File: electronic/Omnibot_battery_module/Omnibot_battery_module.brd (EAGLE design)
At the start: 60 x 213.7 mm, 30 parts, among them IC7 TJA1050T, J1 B1, J3 XT60-M, J4 XT60-M, J7 ATX24RH, J9 RES JUMPER, Y1 CSTCE16M0V53-R0

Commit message: add manip, realseses, fix battery module
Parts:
- moved J11 3.81 mm to (41.9, -8.89)
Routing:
- net GND: track 410.4 -> 415.5 mm
- net N$26: track 42.5 -> 38.7 mm
- net N$25: track 42.6 -> 38.8 mm
- net N$24: track 40.1 -> 36.3 mm
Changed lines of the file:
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@@
 <attribute name="VALUE" x="51.054" y="95.25" size="0.6096" layer="27" font="vector" ratio="20" rot="R90" align="top-left"/>
 </element>
-<element name="J11" library="SparkFun-Connectors" package="1X05" value="" x="45.72" y="-8.89" smashed="yes" rot="R180">
-<attribute name="NAME" x="46.99" y="-10.287" size="0.6096" layer="25" font="vector" ratio="20" rot="R180"/>
-<attribute name="VALUE" x="46.99" y="-6.858" size="0.6096" layer="27" font="vector" ratio="20" rot="R180"/>
+<element name="J11" library="SparkFun-Connectors" package="1X05" value="" x="41.91" y="-8.89" smashed="yes" rot="R180">
+<attribute name="NAME" x="43.18" y="-10.287" size="0.6096" layer="25" font="vector" ratio="20" rot="R180"/>
+<attribute name="VALUE" x="43.18" y="-6.858" size="0.6096" layer="27" font="vector" ratio="20" rot="R180"/>
 </element>
 <element name="J2" library="SparkFun-Connectors" package="MOLEX-1X4" value="" x="37.846" y="54.61" locked="yes" smashed="yes" rot="R270">
@@
 <wire x1="52.705" y1="41.97" x2="52.705" y2="40.005" width="0.5" layer="16"/>
 <wire x1="52.705" y1="40.005" x2="51.3715" y2="38.6715" width="0.5" layer="16"/>
-<wire x1="33.02" y1="1.27" x2="33.02" y2="0.889" width="0.5" layer="16"/>
-<wire x1="45.72" y1="-6.35" x2="45.72" y2="-8.89" width="0.5" layer="16"/>
-<wire x1="33.02" y1="0.889" x2="36.6395" y2="-2.7305" width="0.5" layer="16"/>
-<wire x1="36.6395" y1="-2.7305" x2="42.1005" y2="-2.7305" width="0.5" layer="16"/>
-<wire x1="42.1005" y1="-2.7305" x2="45.72" y2="-6.35" width="0.5" layer="16"/>
+<wire x1="33.02" y1="1.27" x2="33.02" y2="-2.7305" width="0.5" layer="16"/>
+<wire x1="41.91" y1="-6.35" x2="41.91" y2="-8.89" width="0.5" layer="16"/>
+<wire x1="33.02" y1="-2.7305" x2="38.2905" y2="-2.7305" width="0.5" layer="16"/>
+<wire x1="38.2905" y1="-2.7305" x2="41.91" y2="-6.35" width="0.5" layer="16"/>
 <wire x1="22.86" y1="5.08" x2="22.86" y2="2.54" width="0.5" layer="16"/>
 <wire x1="22.86" y1="2.54" x2="24.13" y2="3.81" width="0.5" layer="16"/>
@@
 <wire x1="37.846" y1="54.61" x2="60.96" y2="54.61" width="0.508" layer="16"/>
 <wire x1="60.96" y1="54.61" x2="62.23" y2="53.34" width="0.508" layer="16"/>
-<wire x1="62.23" y1="53.34" x2="62.23" y2="7.62" width="0.508" layer="16"/>
-<wire x1="62.23" y1="7.62" x2="45.72" y2="-8.89" width="0.508" layer="16"/>
+<wire x1="62.23" y1="53.34" x2="62.23" y2="2.54" width="0.508" layer="16"/>
+<wire x1="62.23" y1="2.54" x2="50.8" y2="-8.89" width="0.508" layer="16"/>
+<wire x1="50.8" y1="-8.89" x2="41.91" y2="-8.89" width="0.508" layer="16"/>
 <wire x1="43.859" y1="79.883" x2="43.859" y2="63.5" width="5" layer="16"/>
 <wire x1="43.859" y1="63.5" x2="61.468" y2="63.5" width="5" layer="16"/>
@@
 <wire x1="57.15" y1="26.67" x2="56.261" y2="26.67" width="0.5" layer="16"/>
 <wire x1="20.574" y1="-1.016" x2="21.59" y2="-2.032" width="0.5" layer="16"/>
-<wire x1="36.322" y1="-4.064" x2="34.29" y2="-2.032" width="0.5" layer="16"/>
-<wire x1="43.18" y1="-8.89" x2="43.18" y2="-6.35" width="0.5" layer="16"/>
-<wire x1="21.59" y1="-2.032" x2="34.29" y2="-2.032" width="0.5" layer="16"/>
-<wire x1="43.18" y1="-6.35" x2="40.894" y2="-4.064" width="0.5" layer="16"/>
-<wire x1="40.894" y1="-4.064" x2="36.322" y2="-4.064" width="0.5" layer="16"/>
+<wire x1="32.512" y1="-4.064" x2="30.48" y2="-2.032" width="0.5" layer="16"/>
+<wire x1="39.37" y1="-8.89" x2="39.37" y2="-6.35" width="0.5" layer="16"/>
+<wire x1="21.59" y1="-2.032" x2="30.48" y2="-2.032" width="0.5" layer="16"/>
+<wire x1="39.37" y1="-6.35" x2="37.084" y2="-4.064" width="0.5" layer="16"/>
+<wire x1="37.084" y1="-4.064" x2="32.512" y2="-4.064" width="0.5" layer="16"/>
 <wire x1="22.86" y1="7.62" x2="20.574" y2="7.62" width="0.5" layer="16"/>
 <wire x1="20.574" y1="7.62" x2="20.574" y2="-1.016" width="0.5" layer="16"/>
@@
 <wire x1="50.292" y1="13.208" x2="46.609" y2="13.208" width="0.508" layer="16"/>
 <wire x1="46.609" y1="13.208" x2="41.021" y2="7.62" width="0.508" layer="16"/>
-<wire x1="43.18" y1="-8.89" x2="43.18" y2="-11.43" width="1.27" layer="16"/>
-<wire x1="45.72" y1="-13.97" x2="63.754" y2="-13.97" width="1.27" layer="16"/>
+<wire x1="39.37" y1="-8.89" x2="39.37" y2="-11.43" width="1.27" layer="16"/>
+<wire x1="41.91" y1="-13.97" x2="63.754" y2="-13.97" width="1.27" layer="16"/>
 <wire x1="63.754" y1="-13.97" x2="63.754" y2="56.355" width="1.27" layer="16"/>
 <wire x1="63.754" y1="56.355" x2="44.59259375" y2="56.355" width="1.27" layer="16"/>
@@
 <wire x1="44.59259375" y1="56.355" x2="38.71759375" y2="62.23" width="1.27" layer="16"/>
 <wire x1="27.94" y1="62.23" x2="27.94" y2="77.47" width="1.27" layer="16"/>
-<wire x1="43.18" y1="-11.43" x2="45.72" y2="-13.97" width="1.27" layer="16"/>
+<wire x1="39.37" y1="-11.43" x2="41.91" y2="-13.97" width="1.27" layer="16"/>
 <wire x1="41.021" y1="7.62" x2="33.02" y2="16.51" width="0" layer="19" extent="16-16"/>
 </signal>
@@
 <contactref element="U$1" pad="RX1-1"/>
 <contactref element="J11" pad="3"/>
-<wire x1="39.624" y1="-5.207" x2="40.64" y2="-6.223" width="0.5" layer="16"/>
-<wire x1="40.64" y1="-6.223" x2="40.64" y2="-8.89" width="0.5" layer="16"/>
-<wire x1="36.068" y1="-5.207" x2="33.909" y2="-3.048" width="0.5" layer="16"/>
-<wire x1="36.068" y1="-5.207" x2="39.624" y2="-5.207" width="0.5" layer="16"/>
+<wire x1="35.814" y1="-5.207" x2="36.83" y2="-6.223" width="0.5" layer="16"/>
+<wire x1="36.83" y1="-6.223" x2="36.83" y2="-8.89" width="0.5" layer="16"/>
+<wire x1="32.258" y1="-5.207" x2="30.099" y2="-3.048" width="0.5" layer="16"/>
+<wire x1="32.258" y1="-5.207" x2="35.814" y2="-5.207" width="0.5" layer="16"/>
 <wire x1="21.336" y1="-3.048" x2="19.558" y2="-1.27" width="0.5" layer="16"/>
-<wire x1="33.909" y1="-3.048" x2="21.336" y2="-3.048" width="0.5" layer="16"/>
+<wire x1="30.099" y1="-3.048" x2="21.336" y2="-3.048" width="0.5" layer="16"/>
 <wire x1="19.558" y1="-1.27" x2="19.558" y2="9.398" width="0.5" layer="16"/>
 <wire x1="19.558" y1="9.398" x2="20.32" y2="10.16" width="0.5" layer="16"/>
-<wire x1="20.32" y1="10.16" x2="21.59" y2="10.16" width="0.5" layer="16"/>
-<wire x1="22.86" y1="10.16" x2="21.59" y2="10.16" width="0.5" layer="16"/>
+<wire x1="22.86" y1="10.16" x2="20.32" y2="10.16" width="0.5" layer="16"/>
 </signal>
 <signal name="N$25">
@@
 <wire x1="22.86" y1="12.7" x2="21.59" y2="12.7" width="0.5" layer="16"/>
 <wire x1="18.669" y1="-1.651" x2="21.082" y2="-4.064" width="0.5" layer="16"/>
-<wire x1="21.082" y1="-4.064" x2="33.655" y2="-4.064" width="0.5" layer="16"/>
+<wire x1="21.082" y1="-4.064" x2="29.845" y2="-4.064" width="0.5" layer="16"/>
 <wire x1="18.669" y1="11.176" x2="18.669" y2="-1.651" width="0.5" layer="16"/>
-<wire x1="36.195" y1="-6.604" x2="37.973" y2="-6.604" width="0.5" layer="16"/>
-<wire x1="37.973" y1="-6.604" x2="38.1" y2="-6.731" width="0.5" layer="16"/>
-<wire x1="38.1" y1="-6.731" x2="38.1" y2="-8.89" width="0.5" layer="16"/>
-<wire x1="33.655" y1="-4.064" x2="36.195" y2="-6.604" width="0.5" layer="16"/>
+<wire x1="32.385" y1="-6.604" x2="34.163" y2="-6.604" width="0.5" layer="16"/>
+<wire x1="34.163" y1="-6.604" x2="34.29" y2="-6.731" width="0.5" layer="16"/>
+<wire x1="34.29" y1="-6.731" x2="34.29" y2="-8.89" width="0.5" layer="16"/>
+<wire x1="29.845" y1="-4.064" x2="32.385" y2="-6.604" width="0.5" layer="16"/>
 <wire x1="20.193" y1="12.7" x2="22.86" y2="12.7" width="0.5" layer="16"/>
 <wire x1="18.669" y1="11.176" x2="20.193" y2="12.7" width="0.5" layer="16"/>
@@
 <wire x1="17.78" y1="12.446" x2="17.78" y2="-2.413" width="0.5" layer="16"/>
 <wire x1="17.78" y1="-2.413" x2="20.32" y2="-4.953" width="0.5" layer="16"/>
-<wire x1="20.32" y1="-4.953" x2="33.274" y2="-4.953" width="0.5" layer="16"/>
-<wire x1="33.274" y1="-4.953" x2="35.56" y2="-7.239" width="0.5" layer="16"/>
-<wire x1="35.56" y1="-7.239" x2="35.56" y2="-8.89" width="0.5" layer="16"/>
+<wire x1="20.32" y1="-4.953" x2="29.464" y2="-4.953" width="0.5" layer="16"/>
+<wire x1="29.464" y1="-4.953" x2="31.75" y2="-7.239" width="0.5" layer="16"/>
+<wire x1="31.75" y1="-7.239" x2="31.75" y2="-8.89" width="0.5" layer="16"/>
 </signal>
 <signal name="B2C2">

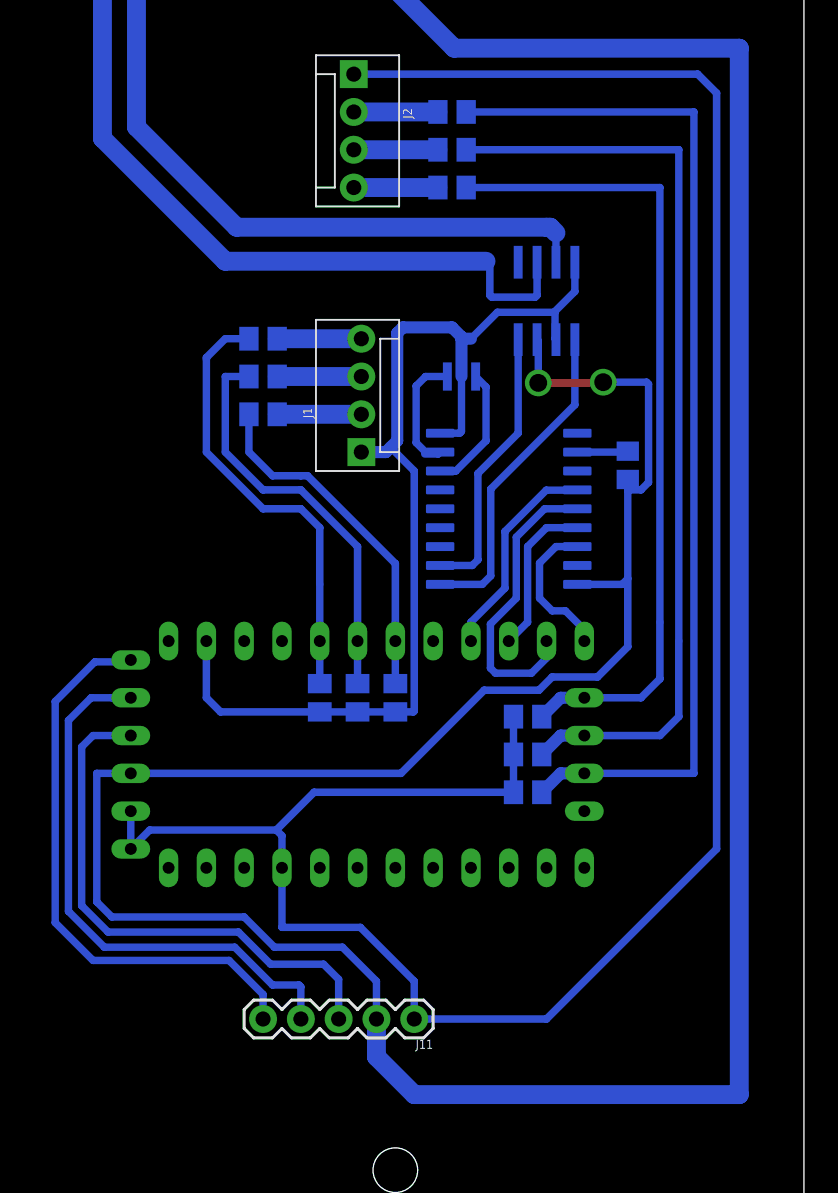
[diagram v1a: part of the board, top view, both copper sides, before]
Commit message: add models for ros
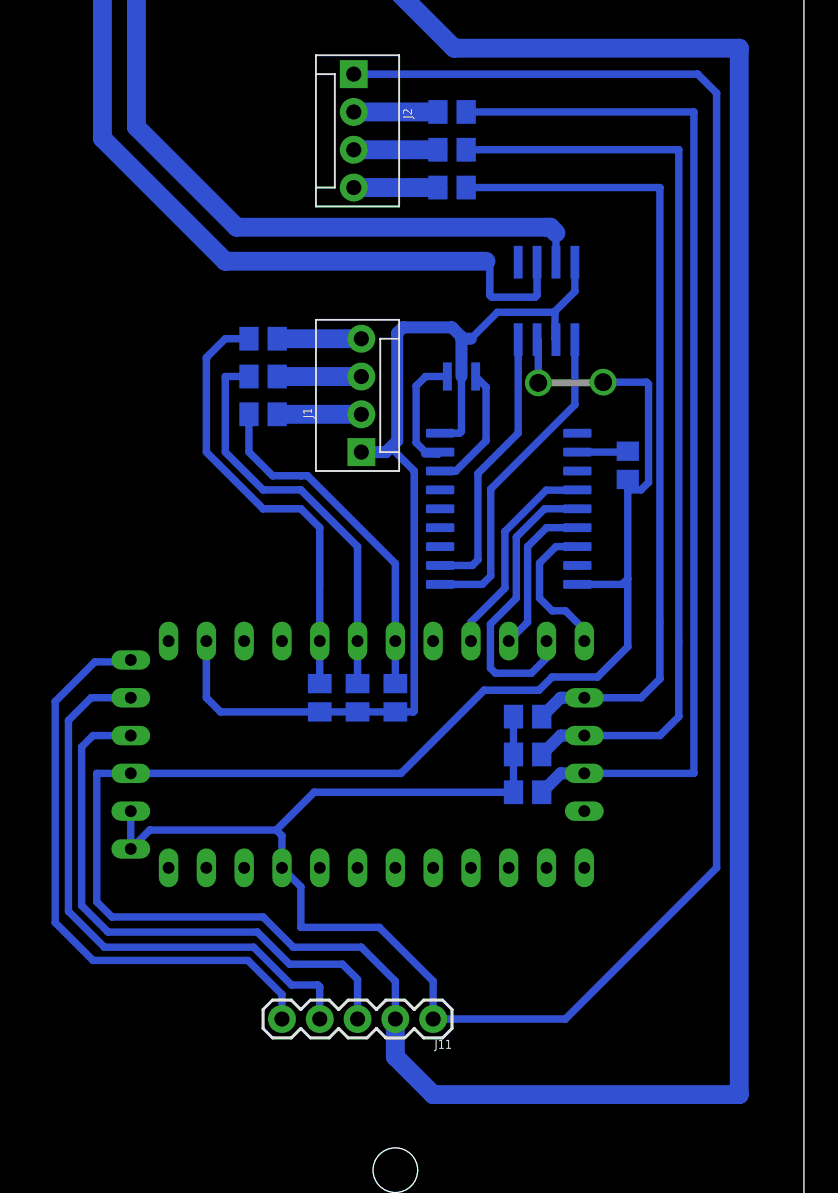
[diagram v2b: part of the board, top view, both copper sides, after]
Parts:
- moved J11 1.27 mm to (43.2, -8.89)
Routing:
- net N$26: track 38.7 -> 40.0 mm
- net N$24: track 36.3 -> 37.5 mm
- net N$25: track 38.8 -> 40.1 mm
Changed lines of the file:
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@@
 <attribute name="VALUE" x="51.054" y="95.25" size="0.6096" layer="27" font="vector" ratio="20" rot="R90" align="top-left"/>
 </element>
-<element name="J11" library="SparkFun-Connectors" package="1X05" value="" x="41.91" y="-8.89" smashed="yes" rot="R180">
-<attribute name="NAME" x="43.18" y="-10.287" size="0.6096" layer="25" font="vector" ratio="20" rot="R180"/>
-<attribute name="VALUE" x="43.18" y="-6.858" size="0.6096" layer="27" font="vector" ratio="20" rot="R180"/>
+<element name="J11" library="SparkFun-Connectors" package="1X05" value="" x="43.18" y="-8.89" smashed="yes" rot="R180">
+<attribute name="NAME" x="44.45" y="-10.287" size="0.6096" layer="25" font="vector" ratio="20" rot="R180"/>
+<attribute name="VALUE" x="44.45" y="-6.858" size="0.6096" layer="27" font="vector" ratio="20" rot="R180"/>
 </element>
 <element name="J2" library="SparkFun-Connectors" package="MOLEX-1X4" value="" x="37.846" y="54.61" locked="yes" smashed="yes" rot="R270">
@@
 <wire x1="52.705" y1="41.97" x2="52.705" y2="40.005" width="0.5" layer="16"/>
 <wire x1="52.705" y1="40.005" x2="51.3715" y2="38.6715" width="0.5" layer="16"/>
-<wire x1="33.02" y1="1.27" x2="33.02" y2="-2.7305" width="0.5" layer="16"/>
-<wire x1="41.91" y1="-6.35" x2="41.91" y2="-8.89" width="0.5" layer="16"/>
-<wire x1="33.02" y1="-2.7305" x2="38.2905" y2="-2.7305" width="0.5" layer="16"/>
-<wire x1="38.2905" y1="-2.7305" x2="41.91" y2="-6.35" width="0.5" layer="16"/>
+<wire x1="33.02" y1="1.27" x2="34.29" y2="0" width="0.5" layer="16"/>
+<wire x1="34.29" y1="0" x2="34.29" y2="-2.7305" width="0.5" layer="16"/>
+<wire x1="43.18" y1="-6.35" x2="43.18" y2="-8.89" width="0.5" layer="16"/>
+<wire x1="34.29" y1="-2.7305" x2="39.5605" y2="-2.7305" width="0.5" layer="16"/>
+<wire x1="39.5605" y1="-2.7305" x2="43.18" y2="-6.35" width="0.5" layer="16"/>
 <wire x1="22.86" y1="5.08" x2="22.86" y2="2.54" width="0.5" layer="16"/>
 <wire x1="22.86" y1="2.54" x2="24.13" y2="3.81" width="0.5" layer="16"/>
@@
 <wire x1="37.846" y1="54.61" x2="60.96" y2="54.61" width="0.508" layer="16"/>
 <wire x1="60.96" y1="54.61" x2="62.23" y2="53.34" width="0.508" layer="16"/>
-<wire x1="62.23" y1="53.34" x2="62.23" y2="2.54" width="0.508" layer="16"/>
-<wire x1="62.23" y1="2.54" x2="50.8" y2="-8.89" width="0.508" layer="16"/>
-<wire x1="50.8" y1="-8.89" x2="41.91" y2="-8.89" width="0.508" layer="16"/>
+<wire x1="62.23" y1="53.34" x2="62.23" y2="1.27" width="0.508" layer="16"/>
+<wire x1="62.23" y1="1.27" x2="52.07" y2="-8.89" width="0.508" layer="16"/>
+<wire x1="52.07" y1="-8.89" x2="43.18" y2="-8.89" width="0.508" layer="16"/>
 <wire x1="43.859" y1="79.883" x2="43.859" y2="63.5" width="5" layer="16"/>
 <wire x1="43.859" y1="63.5" x2="61.468" y2="63.5" width="5" layer="16"/>
@@
 <wire x1="57.15" y1="26.67" x2="56.261" y2="26.67" width="0.5" layer="16"/>
 <wire x1="20.574" y1="-1.016" x2="21.59" y2="-2.032" width="0.5" layer="16"/>
-<wire x1="32.512" y1="-4.064" x2="30.48" y2="-2.032" width="0.5" layer="16"/>
-<wire x1="39.37" y1="-8.89" x2="39.37" y2="-6.35" width="0.5" layer="16"/>
-<wire x1="21.59" y1="-2.032" x2="30.48" y2="-2.032" width="0.5" layer="16"/>
-<wire x1="39.37" y1="-6.35" x2="37.084" y2="-4.064" width="0.5" layer="16"/>
-<wire x1="37.084" y1="-4.064" x2="32.512" y2="-4.064" width="0.5" layer="16"/>
+<wire x1="33.782" y1="-4.064" x2="31.75" y2="-2.032" width="0.5" layer="16"/>
+<wire x1="40.64" y1="-8.89" x2="40.64" y2="-6.35" width="0.5" layer="16"/>
+<wire x1="21.59" y1="-2.032" x2="31.75" y2="-2.032" width="0.5" layer="16"/>
+<wire x1="40.64" y1="-6.35" x2="38.354" y2="-4.064" width="0.5" layer="16"/>
+<wire x1="38.354" y1="-4.064" x2="33.782" y2="-4.064" width="0.5" layer="16"/>
 <wire x1="22.86" y1="7.62" x2="20.574" y2="7.62" width="0.5" layer="16"/>
 <wire x1="20.574" y1="7.62" x2="20.574" y2="-1.016" width="0.5" layer="16"/>
@@
 <wire x1="50.292" y1="13.208" x2="46.609" y2="13.208" width="0.508" layer="16"/>
 <wire x1="46.609" y1="13.208" x2="41.021" y2="7.62" width="0.508" layer="16"/>
-<wire x1="39.37" y1="-8.89" x2="39.37" y2="-11.43" width="1.27" layer="16"/>
-<wire x1="41.91" y1="-13.97" x2="63.754" y2="-13.97" width="1.27" layer="16"/>
+<wire x1="40.64" y1="-8.89" x2="40.64" y2="-11.43" width="1.27" layer="16"/>
+<wire x1="43.18" y1="-13.97" x2="63.754" y2="-13.97" width="1.27" layer="16"/>
 <wire x1="63.754" y1="-13.97" x2="63.754" y2="56.355" width="1.27" layer="16"/>
 <wire x1="63.754" y1="56.355" x2="44.59259375" y2="56.355" width="1.27" layer="16"/>
@@
 <wire x1="44.59259375" y1="56.355" x2="38.71759375" y2="62.23" width="1.27" layer="16"/>
 <wire x1="27.94" y1="62.23" x2="27.94" y2="77.47" width="1.27" layer="16"/>
-<wire x1="39.37" y1="-11.43" x2="41.91" y2="-13.97" width="1.27" layer="16"/>
+<wire x1="40.64" y1="-11.43" x2="43.18" y2="-13.97" width="1.27" layer="16"/>
 <wire x1="41.021" y1="7.62" x2="33.02" y2="16.51" width="0" layer="19" extent="16-16"/>
 </signal>
@@
 <contactref element="U$1" pad="RX1-1"/>
 <contactref element="J11" pad="3"/>
-<wire x1="35.814" y1="-5.207" x2="36.83" y2="-6.223" width="0.5" layer="16"/>
-<wire x1="36.83" y1="-6.223" x2="36.83" y2="-8.89" width="0.5" layer="16"/>
-<wire x1="32.258" y1="-5.207" x2="30.099" y2="-3.048" width="0.5" layer="16"/>
-<wire x1="32.258" y1="-5.207" x2="35.814" y2="-5.207" width="0.5" layer="16"/>
+<wire x1="37.084" y1="-5.207" x2="38.1" y2="-6.223" width="0.5" layer="16"/>
+<wire x1="38.1" y1="-6.223" x2="38.1" y2="-8.89" width="0.5" layer="16"/>
+<wire x1="33.528" y1="-5.207" x2="31.369" y2="-3.048" width="0.5" layer="16"/>
+<wire x1="33.528" y1="-5.207" x2="37.084" y2="-5.207" width="0.5" layer="16"/>
 <wire x1="21.336" y1="-3.048" x2="19.558" y2="-1.27" width="0.5" layer="16"/>
-<wire x1="30.099" y1="-3.048" x2="21.336" y2="-3.048" width="0.5" layer="16"/>
+<wire x1="31.369" y1="-3.048" x2="21.336" y2="-3.048" width="0.5" layer="16"/>
 <wire x1="19.558" y1="-1.27" x2="19.558" y2="9.398" width="0.5" layer="16"/>
 <wire x1="19.558" y1="9.398" x2="20.32" y2="10.16" width="0.5" layer="16"/>
@@
 <wire x1="22.86" y1="12.7" x2="21.59" y2="12.7" width="0.5" layer="16"/>
 <wire x1="18.669" y1="-1.651" x2="21.082" y2="-4.064" width="0.5" layer="16"/>
-<wire x1="21.082" y1="-4.064" x2="29.845" y2="-4.064" width="0.5" layer="16"/>
+<wire x1="21.082" y1="-4.064" x2="31.115" y2="-4.064" width="0.5" layer="16"/>
 <wire x1="18.669" y1="11.176" x2="18.669" y2="-1.651" width="0.5" layer="16"/>
-<wire x1="32.385" y1="-6.604" x2="34.163" y2="-6.604" width="0.5" layer="16"/>
-<wire x1="34.163" y1="-6.604" x2="34.29" y2="-6.731" width="0.5" layer="16"/>
-<wire x1="34.29" y1="-6.731" x2="34.29" y2="-8.89" width="0.5" layer="16"/>
-<wire x1="29.845" y1="-4.064" x2="32.385" y2="-6.604" width="0.5" layer="16"/>
+<wire x1="33.655" y1="-6.604" x2="35.433" y2="-6.604" width="0.5" layer="16"/>
+<wire x1="35.433" y1="-6.604" x2="35.56" y2="-6.731" width="0.5" layer="16"/>
+<wire x1="35.56" y1="-6.731" x2="35.56" y2="-8.89" width="0.5" layer="16"/>
+<wire x1="31.115" y1="-4.064" x2="33.655" y2="-6.604" width="0.5" layer="16"/>
 <wire x1="20.193" y1="12.7" x2="22.86" y2="12.7" width="0.5" layer="16"/>
 <wire x1="18.669" y1="11.176" x2="20.193" y2="12.7" width="0.5" layer="16"/>
@@
 <wire x1="17.78" y1="12.446" x2="17.78" y2="-2.413" width="0.5" layer="16"/>
 <wire x1="17.78" y1="-2.413" x2="20.32" y2="-4.953" width="0.5" layer="16"/>
-<wire x1="20.32" y1="-4.953" x2="29.464" y2="-4.953" width="0.5" layer="16"/>
-<wire x1="29.464" y1="-4.953" x2="31.75" y2="-7.239" width="0.5" layer="16"/>
-<wire x1="31.75" y1="-7.239" x2="31.75" y2="-8.89" width="0.5" layer="16"/>
+<wire x1="20.32" y1="-4.953" x2="30.734" y2="-4.953" width="0.5" layer="16"/>
+<wire x1="30.734" y1="-4.953" x2="33.02" y2="-7.239" width="0.5" layer="16"/>
+<wire x1="33.02" y1="-7.239" x2="33.02" y2="-8.89" width="0.5" layer="16"/>
 </signal>
 <signal name="B2C2">
